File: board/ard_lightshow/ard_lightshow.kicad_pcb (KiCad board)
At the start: 2 copper layers, 38.1 x 68.6 mm, 10 parts, among them U0 arduino_nano, U1 rf24, U2 mic_electret, U3 wire_power

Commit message: Uniformized via sizes and increased to 2mm copper for easier manufacture.
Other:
- net class Default: via_drill 1 -> 0.8
- net class Power: via_drill 1 -> 0.8
- board text added: "REV 1.1"
- board text removed: "REV 1.0"

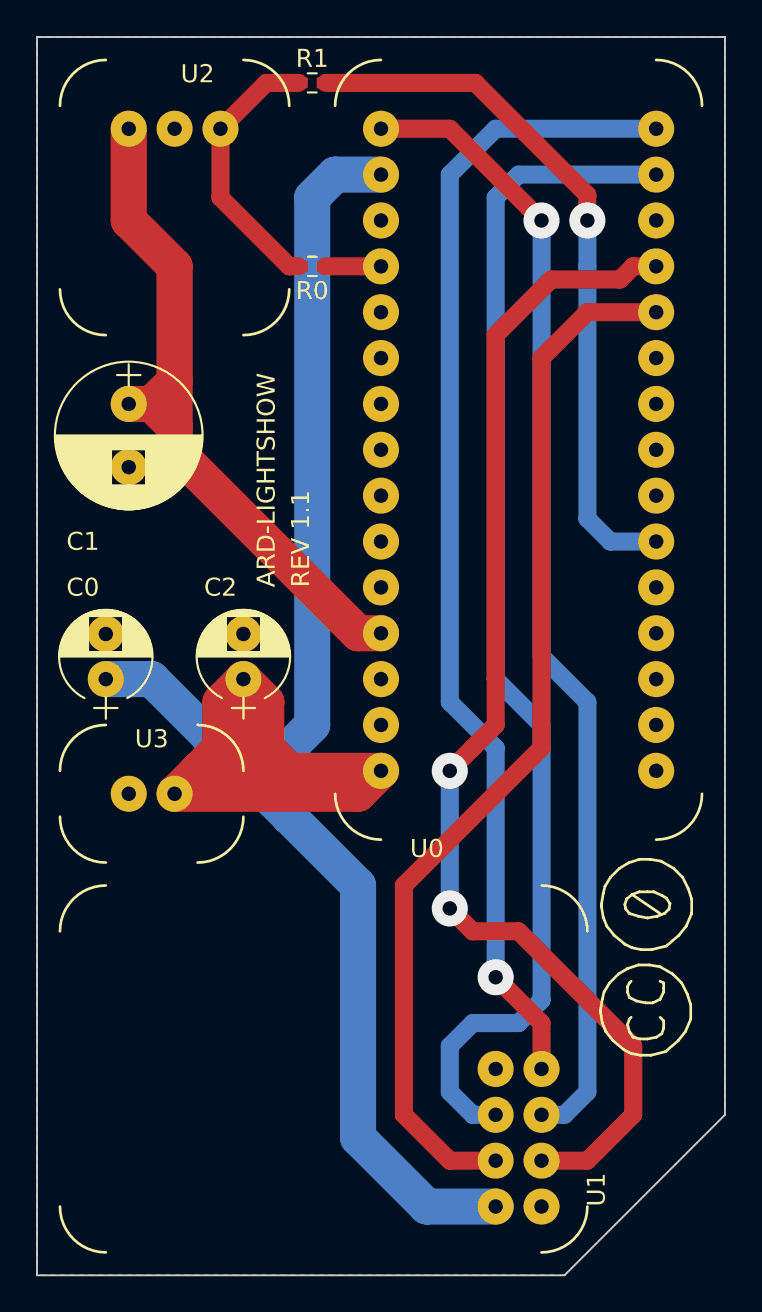
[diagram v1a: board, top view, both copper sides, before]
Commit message: Bumped up isolation and decals/solder mask to aid in micro-batch CNC milling.
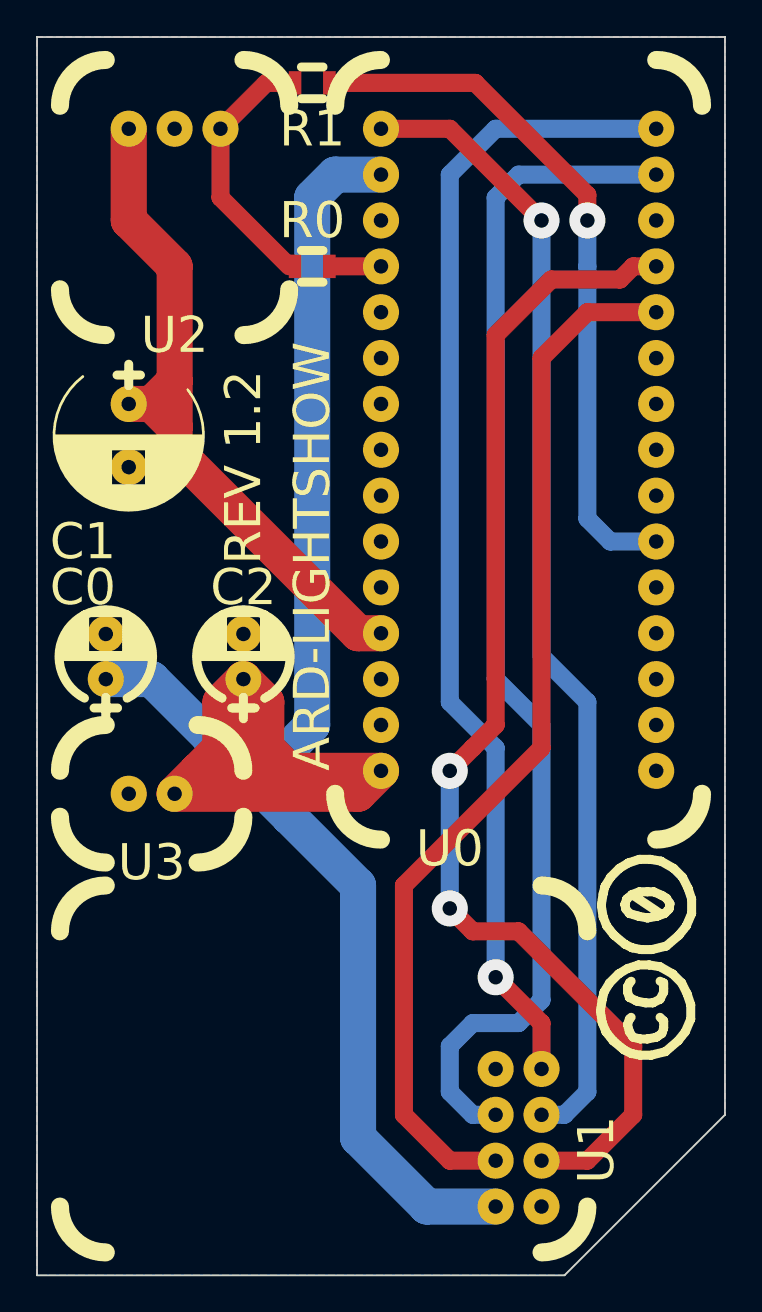
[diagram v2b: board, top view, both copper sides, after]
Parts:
- R0, R1: footprint Resistors_SMD:R_0402 -> Resistors_SMD:R_0805
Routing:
- net Net-(R0-Pad2): track 15.1 -> 14.1 mm
- net /IR_OUT: track 39.3 -> 38.8 mm
- net /MIC_OUT: track 3.06 -> 2.54 mm
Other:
- board text added: "REV 1.2"
- board text removed: "REV 1.1"

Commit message: Updated PCB vias to 1.0mm/0.6mm drill holes for ease of via rivetting.
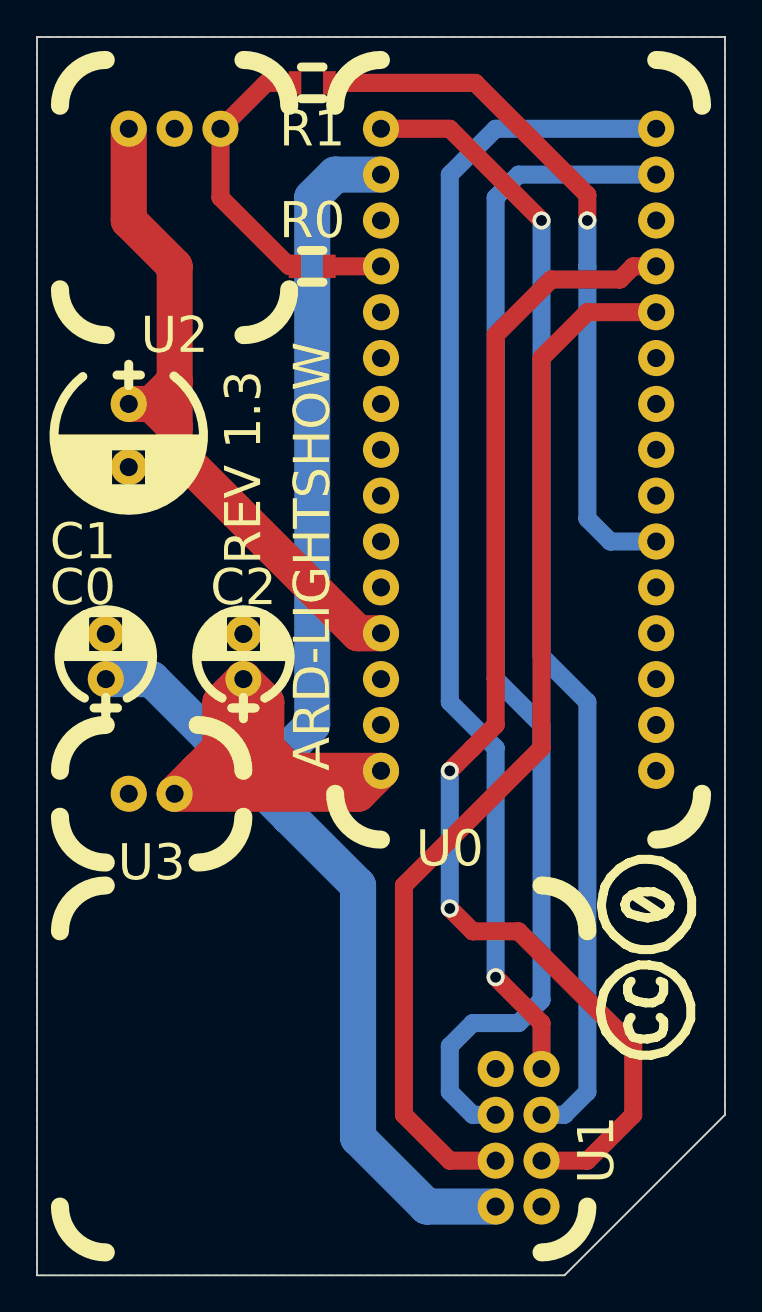
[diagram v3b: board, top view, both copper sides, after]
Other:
- net class Default: via_drill 0.8 -> 1
- net class Power: via_drill 0.8 -> 1
- rule trace_min: 0.2 -> 0.5
- rule via_min_drill: 0.3 -> 0.6
- rule via_min_size: 0.4 -> 1
- board text added: "REV 1.3"
- board text removed: "REV 1.2"
